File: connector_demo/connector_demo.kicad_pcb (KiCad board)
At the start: 2 copper layers, 104 x 60.5 mm, 7 parts, among them J1 PicoBlade 8-wide, J2 PicoLock 8-wide, J3 MicroLock 4-wide, J4 Conn_01x08_Pin, J5 Conn_01x08_Pin, J6 Conn_01x04_Pin

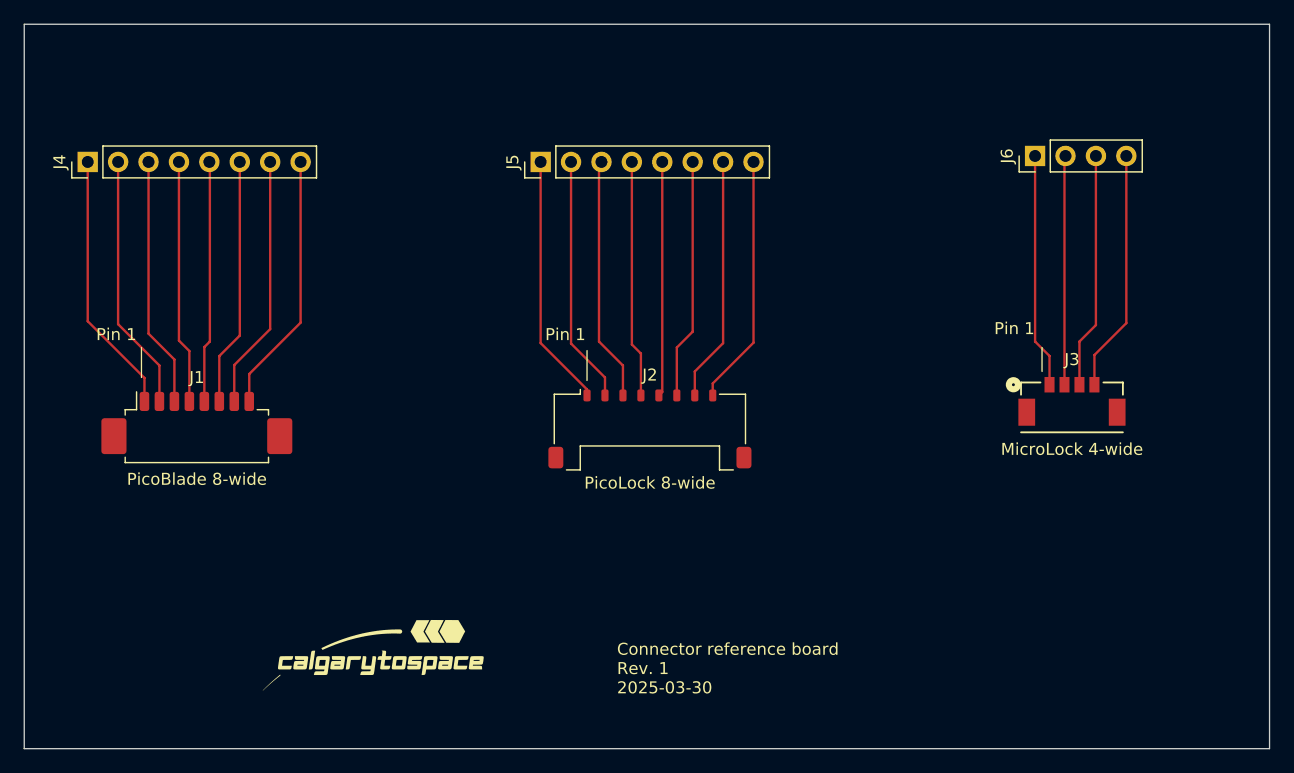
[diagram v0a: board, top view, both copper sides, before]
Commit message: update microlock to 8 pin, confirmed pin 1
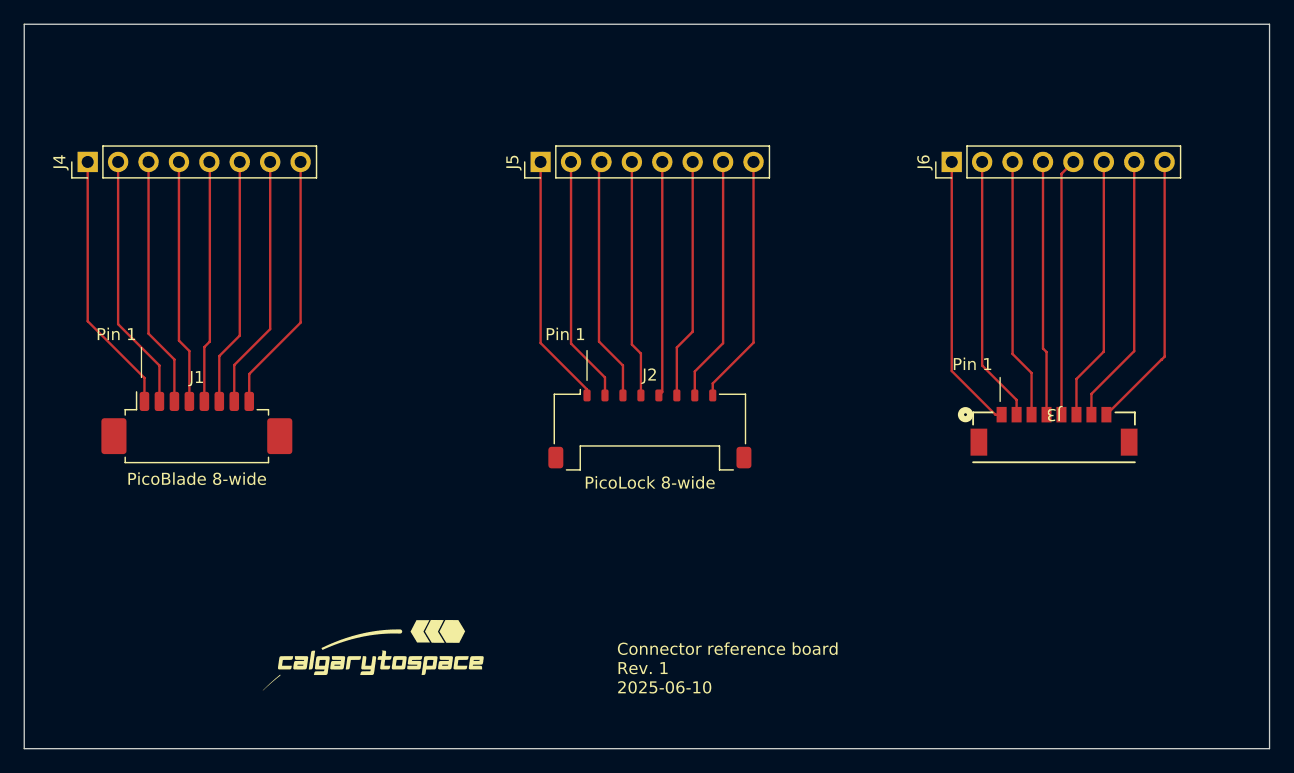
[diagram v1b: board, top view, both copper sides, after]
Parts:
- J3: value MicroLock 4-wide -> MicroLock 8-wide; footprint microlock:CONN04_5055670471_MOL -> microlock:CONN08_5055670871_MOL
- J6: value Conn_01x04_Pin -> Conn_01x08_Pin; footprint Connector_PinHeader_2.54mm:PinHeader_1x04_P2.54mm_Vertical -> Connector_PinHeader_2.54mm:PinHeader_1x08_P2.54mm_Vertical
- moved J6 6.98 mm to (170.0, 70.0)
- moved J3 2.92 mm to (178.5, 93.0)
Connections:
- J3 pad 5: (no net) -> Net-(J3-Pin_5)
- J3 pad 6: (no net) -> Net-(J3-Pin_6)
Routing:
- net Net-(J3-Pin_8): track 0.00 -> 23.1 mm
- net Net-(J3-Pin_7): track 0.00 -> 22.6 mm
- net Net-(J3-Pin_6): track 0.00 -> 22.1 mm
- net Net-(J3-Pin_5): track 0.00 -> 21.5 mm
- net Net-(J3-Pin_1): track 19.7 -> 23.1 mm
- net Net-(J3-Pin_2): track 19.1 -> 22.3 mm
- net Net-(J3-Pin_3): track 19.7 -> 21.8 mm
- net Net-(J3-Pin_4): track 20.2 -> 21.2 mm
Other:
- board text added: "Connector reference board Rev. 1 2025-06-10"
- board text removed: "Connector reference board Rev. 1 2025-03-30"
